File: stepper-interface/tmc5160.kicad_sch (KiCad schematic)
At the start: 30 parts, among them J401 Molex_Pico-SPOX_Horizontal, J402 Molex_Pico-Clasp_Horizontal, U401 TMC5160A-WA, U402 MAX6816, X401 16MHz

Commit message: First attempt at production files
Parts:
- C401, C403, C404, C408, C413, C417: Comment (none) -> 0.1 µF ±10% 100V Ceramic Capacitor X5R 0402 (1005 Metric)
- C402: Comment (none) -> 0.022 µF ±10% 100V Ceramic Capacitor X7R 0603 (1608 Metric)
- C405: Comment (none) -> 0.47 µF ±10% 35V Ceramic Capacitor X5R 0402 (1005 Metric)
- C406, C407: Comment (none) -> 2.2 µF ±10% 35V Ceramic Capacitor X5R 0402 (1005 Metric)
- C409, C410, C411, C412: Comment (none) -> 0.22 µF ±10% 25V Ceramic Capacitor X6S 0402 (1005 Metric)
- C414, C415: Comment (none) -> 2.2 µF ±10% 100V Ceramic Capacitor X7T 0805 (2012 Metric)
- C416: Comment (none) -> 220 µF 50 V Aluminum - Polymer Capacitors Radial, Can - SMD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
- D401: Comment (none) -> 77.4V Clamp 2.6A Ipp Tvs Diode Surface Mount SOD-123F; Package (none) -> SOD-123F
- J401: Comment (none) -> Connector Header Surface Mount, Right Angle 4 position 0.05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
- J402: Comment (none) -> Connector Header Surface Mount, Right Angle 2 position 0.03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
- R401: Comment (none) -> 2.2 Ohms ±5% 0.1W, 1/10W Chip Resistor 0402 (1005 Metric) A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
- R402, R403, R406, R407: Comment (none) -> 47 Ohms ±1% 0.063W, 1/16W Chip Resistor 0402 (1005 Metric) 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
- R404, R405: Comment (none) -> 150 mOhms ±1% 1W Chip Resistor 1206 (3216 Metric) Automotiv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
- U401: Comment (none) -> Bipolar Motor Driver Power MOSFET SPI, Step/Direction 56-QF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
- U402: Comment (none) -> Switch Debouncer SOT-143-4
- X401: Comment (none) -> 16 MHz XO (Standard) HCMOS Oscillator 3.3V Enable/Disable 4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
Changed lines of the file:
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@@
       (effects (font (size 1.524 1.524)) hide)
+    )
+    (property "Comment" "0.22 µF ±10% 25V Ceramic Capacitor X6S 0402 (1005 Metric)" (at 226.06 40.64 0)
+      (effects (font (size 1.27 1.27)) hide)
     )
     (pin "1")
@@
       (effects (font (size 1.524 1.524)) hide)
     )
+    (property "Comment" "47 Ohms ±1% 0.063W, 1/16W Chip Resistor 0402 (1005 Metric) Automotive AEC-Q200 Thick Film" (at 97.79 129.54 0)
+      (effects (font (size 1.27 1.27)) hide)
+    )
     (pin "1")
     (pin "2")
@@
       (effects (font (size 1.524 1.524)) hide)
     )
+    (property "Comment" "0.1 µF ±10% 100V Ceramic Capacitor X5R 0402 (1005 Metric)" (at 187.96 40.64 0)
+      (effects (font (size 1.27 1.27)) hide)
+    )
     (pin "2")
     (pin "1")
@@
     (property "Synopsis" "CAP CER 0.22UF 25V X6S" (at 208.28 30.48 0)
       (effects (font (size 1.524 1.524)) hide)
+    )
+    (property "Comment" "0.22 µF ±10% 25V Ceramic Capacitor X6S 0402 (1005 Metric)" (at 200.66 40.64 0)
+      (effects (font (size 1.27 1.27)) hide)
     )
     (pin "1")
@@
       (effects (font (size 1.524 1.524)) hide)
     )
+    (property "Comment" "2.2 µF ±10% 35V Ceramic Capacitor X5R 0402 (1005 Metric)" (at 162.56 40.64 0)
+      (effects (font (size 1.27 1.27)) hide)
+    )
     (pin "2")
     (pin "1")
@@
       (effects (font (size 1.27 1.27)) hide)
     )
+    (property "Comment" "Connector Header Surface Mount, Right Angle 4 position 0.059\" (1.50mm)" (at 276.86 125.73 0)
+      (effects (font (size 1.27 1.27)) hide)
+    )
     (pin "1")
     (pin "2")
@@
     (property "Synopsis" "IC SWITCH DEBOUNCER" (at 54.61 191.77 0)
       (effects (font (size 1.524 1.524)) hide)
+    )
+    (property "Comment" "Switch Debouncer SOT-143-4" (at 54.61 175.26 0)
+      (effects (font (size 1.27 1.27)) hide)
     )
     (pin "1")
@@
       (effects (font (size 1.524 1.524)) hide)
     )
+    (property "Comment" "0.1 µF ±10% 100V Ceramic Capacitor X5R 0402 (1005 Metric)" (at 48.26 40.64 0)
+      (effects (font (size 1.27 1.27)) hide)
+    )
     (pin "2")
     (pin "1")
@@
       (effects (font (size 1.524 1.524)) hide)
     )
+    (property "Comment" "0.22 µF ±10% 25V Ceramic Capacitor X6S 0402 (1005 Metric)" (at 213.36 40.64 0)
+      (effects (font (size 1.27 1.27)) hide)
+    )
     (pin "1")
     (pin "2")
@@
     (property "Synopsis" "CAP CER 0.1UF 100V X5R" (at 170.18 55.88 0)
       (effects (font (size 1.524 1.524)) hide)
+    )
+    (property "Comment" "0.1 µF ±10% 100V Ceramic Capacitor X5R 0402 (1005 Metric)" (at 162.56 66.04 0)
+      (effects (font (size 1.27 1.27)) hide)
     )
     (pin "2")
@@
     )
     (property "Synopsis" "IC MTR DRVR BIPOLAR 8-60V" (at 54.61 109.22 0)
+      (effects (font (size 1.27 1.27)) hide)
+    )
+    (property "Comment" "Bipolar Motor Driver Power MOSFET SPI, Step/Direction 56-QFN (8x8)" (at 54.61 109.22 0)
       (effects (font (size 1.27 1.27)) hide)
     )
@@
       (effects (font (size 1.524 1.524)) hide)
     )
+    (property "Comment" "0.022 µF ±10% 100V Ceramic Capacitor X7R 0603 (1608 Metric)" (at 99.06 40.64 0)
+      (effects (font (size 1.27 1.27)) hide)
+    )
     (pin "1")
     (pin "2")
@@
       (effects (font (size 1.524 1.524)) hide)
     )
+    (property "Comment" "2.2 µF ±10% 100V Ceramic Capacitor X7T 0805 (2012 Metric)" (at 187.96 66.04 0)
+      (effects (font (size 1.27 1.27)) hide)
+    )
     (pin "2")
     (pin "1")
@@
       (effects (font (size 1.524 1.524)) hide)
     )
+    (property "Comment" "47 Ohms ±1% 0.063W, 1/16W Chip Resistor 0402 (1005 Metric) Automotive AEC-Q200 Thick Film" (at 97.79 111.76 0)
+      (effects (font (size 1.27 1.27)) hide)
+    )
     (pin "1")
     (pin "2")
@@
       (effects (font (size 1.524 1.524)) hide)
     )
+    (property "Comment" "150 mOhms ±1% 1W Chip Resistor 1206 (3216 Metric) Automotive AEC-Q200, Current Sense Thick Film" (at 106.68 120.65 0)
+      (effects (font (size 1.27 1.27)) hide)
+    )
     (pin "2")
     (pin "1")
@@
     )
     (property "Vendor Part Number" "F5832CT-ND" (at 149.86 66.04 0)
+      (effects (font (size 1.27 1.27)) hide)
+    )
+    (property "Comment" "77.4V Clamp 2.6A Ipp Tvs Diode Surface Mount SOD-123F" (at 149.86 66.04 0)
+      (effects (font (size 1.27 1.27)) hide)
+    )
+    (property "Package" " SOD-123F" (at 149.86 66.04 0)
       (effects (font (size 1.27 1.27)) hide)
     )
@@
     )
     (property "Synopsis" "XTAL OSC XO 16.0000MHZ HCMOS SMD" (at 71.12 40.64 0)
+      (effects (font (size 1.27 1.27)) hide)
+    )
+    (property "Comment" "16 MHz XO (Standard) HCMOS Oscillator 3.3V Enable/Disable 4-SMD, No Lead" (at 71.12 40.64 0)
       (effects (font (size 1.27 1.27)) hide)
     )
@@
       (effects (font (size 1.27 1.27)) hide)
     )
+    (property "Comment" "Connector Header Surface Mount, Right Angle 2 position 0.039\" (1.00mm)" (at 101.6 177.8 0)
+      (effects (font (size 1.27 1.27)) hide)
+    )
     (pin "2")
     (pin "1")
@@
       (effects (font (size 1.524 1.524)) hide)
     )
+    (property "Comment" "47 Ohms ±1% 0.063W, 1/16W Chip Resistor 0402 (1005 Metric) Automotive AEC-Q200 Thick Film" (at 128.27 111.76 0)
+      (effects (font (size 1.27 1.27)) hide)
+    )
     (pin "1")
     (pin "2")
@@
       (effects (font (size 1.524 1.524)) hide)
     )
+    (property "Comment" "0.47 µF ±10% 35V Ceramic Capacitor X5R 0402 (1005 Metric)" (at 137.16 40.64 0)
+      (effects (font (size 1.27 1.27)) hide)
+    )
     (pin "2")
     (pin "1")
@@
       (effects (font (size 1.27 1.27)) hide)
     )
+    (property "Comment" "220 µF 50 V Aluminum - Polymer Capacitors Radial, Can - SMD 13mOhm 4000 Hrs @ 125°C" (at 200.66 66.04 0)
+      (effects (font (size 1.27 1.27)) hide)
+    )
     (pin "1")
     (pin "2")
@@
     (property "Synopsis" "CAP CER 0.22UF 25V X6S" (at 246.38 30.48 0)
       (effects (font (size 1.524 1.524)) hide)
+    )
+    (property "Comment" "0.22 µF ±10% 25V Ceramic Capacitor X6S 0402 (1005 Metric)" (at 238.76 40.64 0)
+      (effects (font (size 1.27 1.27)) hide)
     )
     (pin "1")
@@
       (effects (font (size 1.524 1.524)) hide)
     )
+    (property "Comment" "47 Ohms ±1% 0.063W, 1/16W Chip Resistor 0402 (1005 Metric) Automotive AEC-Q200 Thick Film" (at 128.27 129.54 0)
+      (effects (font (size 1.27 1.27)) hide)
+    )
     (pin "1")
     (pin "2")
@@
       (effects (font (size 1.524 1.524)) hide)
     )
+    (property "Comment" "2.2 Ohms ±5% 0.1W, 1/10W Chip Resistor 0402 (1005 Metric) Automotive AEC-Q200 Thick Film" (at 149.86 40.64 0)
+      (effects (font (size 1.27 1.27)) hide)
+    )
     (pin "1")
     (pin "2")
@@
     (property "Synopsis" "CAP CER 0.1UF 100V X5R" (at 132.08 30.48 0)
       (effects (font (size 1.524 1.524)) hide)
+    )
+    (property "Comment" "0.1 µF ±10% 100V Ceramic Capacitor X5R 0402 (1005 Metric)" (at 124.46 40.64 0)
+      (effects (font (size 1.27 1.27)) hide)
     )
     (pin "2")
@@
       (effects (font (size 1.524 1.524)) hide)
     )
+    (property "Comment" "150 mOhms ±1% 1W Chip Resistor 1206 (3216 Metric) Automotive AEC-Q200, Current Sense Thick Film" (at 137.16 120.65 0)
+      (effects (font (size 1.27 1.27)) hide)
+    )
     (pin "2")
     (pin "1")
@@
       (effects (font (size 1.524 1.524)) hide)
     )
+    (property "Comment" "2.2 µF ±10% 35V Ceramic Capacitor X5R 0402 (1005 Metric)" (at 175.26 40.64 0)
+      (effects (font (size 1.27 1.27)) hide)
+    )
     (pin "2")
     (pin "1")
@@
       (effects (font (size 1.524 1.524)) hide)
     )
+    (property "Comment" "2.2 µF ±10% 100V Ceramic Capacitor X7T 0805 (2012 Metric)" (at 175.26 66.04 0)
+      (effects (font (size 1.27 1.27)) hide)
+    )
     (pin "2")
     (pin "1")
@@
     (property "Synopsis" "CAP CER 0.1UF 100V X5R" (at 119.38 30.48 0)
       (effects (font (size 1.524 1.524)) hide)
+    )
+    (property "Comment" "0.1 µF ±10% 100V Ceramic Capacitor X5R 0402 (1005 Metric)" (at 111.76 40.64 0)
+      (effects (font (size 1.27 1.27)) hide)
     )
     (pin "2")
@@
       (effects (font (size 1.524 1.524)) hide)
     )
-    (pin "2")
+    (property "Comment" "0.1 µF ±10% 100V Ceramic Capacitor X5R 0402 (1005 Metric)" (at 25.4 175.26 0)
+      (effects (font (size 1.27 1.27)) hide)
+    )
+    (pin "2")

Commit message: Update schematic fields
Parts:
- C401, C403, C404, C408, C413, C417: Comment 0.1 µF ±10% 100V Ceramic Capacitor X5R 0402 (1005 Metric) -> Murata Electronics GRM155R62A104KE14D 0.1 µF ±10% 100V Cera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; LCSC (none) -> C162178
- C402: Comment 0.022 µF ±10% 100V Ceramic Capacitor X7R 0603 (1608 Metric) -> Murata Electronics GCM188R72A223KA37D 0.022 µF ±10% 100V Ce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; LCSC (none) -> C161234
- C405: Comment 0.47 µF ±10% 35V Ceramic Capacitor X5R 0402 (1005 Metric) -> Murata Electronics GRT155R6YA474KE01D 0.47 µF ±10% 35V Cera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; LCSC (none) -> C711580
- C406, C407: Comment 2.2 µF ±10% 35V Ceramic Capacitor X5R 0402 (1005 Metric) -> TDK Corporation C1005X5R1V225K050BC 2.2 µF ±10% 35V Ceramic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; LCSC (none) -> C2167643
- C409, C410, C411, C412: Comment 0.22 µF ±10% 25V Ceramic Capacitor X6S 0402 (1005 Metric) -> Murata Electronics GRT155C81E224KE01D 0.22 µF ±10% 25V Cera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; LCSC (none) -> C126623
- C414, C415: Comment 2.2 µF ±10% 100V Ceramic Capacitor X7T 0805 (2012 Metric) -> Murata Electronics GRT21BD72A225KE13K 2.2 µF ±10% 100V Cera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
- C416: Comment 220 µF 50 V Aluminum - Polymer Capacitors Radial, Can - SMD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 -> Panasonic Electronic Components EEH-ZS1H221V 220 µF 50 V Al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
- D401: Comment 77.4V Clamp 2.6A Ipp Tvs Diode Surface Mount SOD-123F -> Littelfuse Inc. SMF48A 77.4V Clamp 2.6A Ipp Tvs Diode Surfa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; LCSC (none) -> C1509577
- J401: Comment Connector Header Surface Mount, Right Angle 4 position 0.05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 -> Molex 0874380443 Connector Header Surface Mount, Right Angl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; LCSC (none) -> C564208
- J402: Comment Connector Header Surface Mount, Right Angle 2 position 0.03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 -> Molex 5015680207 Connector Header Surface Mount, Right Angl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; LCSC (none) -> C505123
- R401: Comment 2.2 Ohms ±5% 0.1W, 1/10W Chip Resistor 0402 (1005 Metric) A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 -> Panasonic Electronic Components ERJ-2GEJ2R2X 2.2 Ohms ±5% 0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
- R402, R403, R406, R407: Comment 47 Ohms ±1% 0.063W, 1/16W Chip Resistor 0402 (1005 Metric) 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 -> Stackpole Electronics Inc RMCF0402FT47R0 47 Ohms ±1% 0.063W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; LCSC (none) -> C2479306
- R404, R405: Comment 150 mOhms ±1% 1W Chip Resistor 1206 (3216 Metric) Automotiv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 -> Delta Electronics/Cyntec VSRP1206S1-R150F 150 mOhms ±1% 1W 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; LCSC (none) -> C4090676
- U401: Comment Bipolar Motor Driver Power MOSFET SPI, Step/Direction 56-QF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 -> Analog Devices Inc. TMC5160A-WA Bipolar Motor Driver Power 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; LCSC (none) -> C1161714
- U402: Comment Switch Debouncer SOT-143-4 -> Analog Devices Inc./Maxim Integrated MAX6816EUS+T Switch De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; LCSC (none) -> C41637
- X401: Comment 16 MHz XO (Standard) HCMOS Oscillator 3.3V Enable/Disable 4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 -> ECS Inc. ECS-2520S33-160-FN-TR 16 MHz XO (Standard) HCMOS O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; LCSC (none) -> C2451298

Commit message: Add jlcpcb fabrication files
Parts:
- J402: Manufactuer Part Number 5015680207 -> (none); Manufacturer Part Number (none) -> 5015680207
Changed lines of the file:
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@@
       (effects (font (size 1.27 1.27)) hide)
     )
-    (property "Manufactuer Part Number" "5015680207" (at 101.6 203.2 0)
+    (property "Manufacturer Part Number" "5015680207" (at 101.6 203.2 0)
       (effects (font (size 1.27 1.27)) hide)
     )

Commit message: Update LCSC part numbers
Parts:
- C414, C415: Comment Murata Electronics GRT21BD72A225KE13K 2.2 µF ±10% 100V Cera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 -> Murata Electronics GRM21BD72A225KE01L 2.2 µF ±10% 100V Cera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; LCSC (none) -> C2981733; Manufacturer Part Number GRT21BD72A225KE13K -> GRM21BD72A225KE01L; Vendor Part Number 490-GRT21BD72A225KE13KCT-ND -> 490-GRM21BD72A225KE01LCT-ND
- C416: LCSC (none) -> C454279
- R401: LCSC (none) -> C412897
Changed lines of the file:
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@@
   (title_block
     (title "stepper-interface")
-    (date "2024-05-08")
+    (date "2024-05-09")
     (rev "1.0")
     (company "Howard Hughes Medical Institute")
@@
       (effects (font (size 1.524 1.524)) hide)
     )
-    (property "Vendor Part Number" "490-GRT21BD72A225KE13KCT-ND" (at 193.04 58.42 0)
+    (property "Vendor Part Number" "490-GRM21BD72A225KE01LCT-ND" (at 193.04 58.42 0)
       (effects (font (size 1.524 1.524)) hide)
     )
@@
       (effects (font (size 1.27 1.27)) hide)
     )
-    (property "Manufacturer Part Number" "GRT21BD72A225KE13K" (at 187.96 66.04 0)
+    (property "Manufacturer Part Number" "GRM21BD72A225KE01L" (at 187.96 66.04 0)
       (effects (font (size 1.27 1.27)) hide)
     )
@@
       (effects (font (size 1.524 1.524)) hide)
     )
-    (property "Comment" "Murata Electronics GRT21BD72A225KE13K 2.2 µF ±10% 100V Ceramic Capacitor X7T 0805 (2012 Metric)" (at 187.96 66.04 0)
-      (effects (font (size 1.27 1.27)) hide)
-    )
-    (property "LCSC" "" (at 187.96 66.04 0)
+    (property "Comment" "Murata Electronics GRM21BD72A225KE01L 2.2 µF ±10% 100V Ceramic Capacitor X7T 0805 (2012 Metric)" (at 187.96 66.04 0)
+      (effects (font (size 1.27 1.27)) hide)
+    )
+    (property "LCSC" "C2981733" (at 187.96 66.04 0)
       (effects (font (size 1.27 1.27)) hide)
     )
@@
       (effects (font (size 1.27 1.27)) hide)
     )
-    (property "LCSC" "" (at 200.66 66.04 0)
+    (property "LCSC" "C454279" (at 200.66 66.04 0)
       (effects (font (size 1.27 1.27)) hide)
     )
@@
       (effects (font (size 1.27 1.27)) hide)
     )
-    (property "LCSC" "" (at 149.86 40.64 0)
+    (property "LCSC" "C412897" (at 149.86 40.64 0)
       (effects (font (size 1.27 1.27)) hide)
     )
@@
       (effects (font (size 1.524 1.524)) hide)
     )
-    (property "Vendor Part Number" "490-GRT21BD72A225KE13KCT-ND" (at 180.34 58.42 0)
+    (property "Vendor Part Number" "490-GRM21BD72A225KE01LCT-ND" (at 180.34 58.42 0)
       (effects (font (size 1.524 1.524)) hide)
     )
@@
       (effects (font (size 1.27 1.27)) hide)
     )
-    (property "Manufacturer Part Number" "GRT21BD72A225KE13K" (at 175.26 66.04 0)
+    (property "Manufacturer Part Number" "GRM21BD72A225KE01L" (at 175.26 66.04 0)
       (effects (font (size 1.27 1.27)) hide)
     )
@@
       (effects (font (size 1.524 1.524)) hide)
     )
-    (property "Comment" "Murata Electronics GRT21BD72A225KE13K 2.2 µF ±10% 100V Ceramic Capacitor X7T 0805 (2012 Metric)" (at 175.26 66.04 0)
-      (effects (font (size 1.27 1.27)) hide)
-    )
-    (property "LCSC" "" (at 175.26 66.04 0)
-      (effects (font (size 1.27 1.27)) hide)
-    )
+    (property "Comment" "Murata Electronics GRM21BD72A225KE01L 2.2 µF ±10% 100V Ceramic Capacitor X7T 0805 (2012 Metric)" (at 175.26 66.04 0)
+      (effects (font (size 1.27 1.27)) hide)
+    )
+    (property "LCSC" "C2981733" (at 175.26 66.04 0)
+      (effects (font (size 1.27 1.27)) hide)
+    )

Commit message: Switch LEDs
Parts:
- C401, C403, C404, C408, C413, C417: Comment Murata Electronics GRM155R62A104KE14D 0.1 µF ±10% 100V Cera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 -> (none)
- C402: Comment Murata Electronics GCM188R72A223KA37D 0.022 µF ±10% 100V Ce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 -> (none)
- C405: Comment Murata Electronics GRT155R6YA474KE01D 0.47 µF ±10% 35V Cera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 -> (none)
- C406, C407: Comment TDK Corporation C1005X5R1V225K050BC 2.2 µF ±10% 35V Ceramic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 -> (none)
- C409, C410, C411, C412: Comment Murata Electronics GRT155C81E224KE01D 0.22 µF ±10% 25V Cera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 -> (none)
- C414, C415: Comment Murata Electronics GRM21BD72A225KE01L 2.2 µF ±10% 100V Cera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 -> (none)
- C416: Comment Panasonic Electronic Components EEH-ZS1H221V 220 µF 50 V Al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 -> (none)
- D401: Comment Littelfuse Inc. SMF48A 77.4V Clamp 2.6A Ipp Tvs Diode Surfa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 -> (none)
- J401: Comment Molex 0874380443 Connector Header Surface Mount, Right Angl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 -> (none)
- J402: Comment Molex 5015680207 Connector Header Surface Mount, Right Angl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 -> (none)
- R401: Comment Panasonic Electronic Components ERJ-2GEJ2R2X 2.2 Ohms ±5% 0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 -> (none)
- R402, R403, R406, R407: Comment Stackpole Electronics Inc RMCF0402FT47R0 47 Ohms ±1% 0.063W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 -> (none)
- R404, R405: Comment Delta Electronics/Cyntec VSRP1206S1-R150F 150 mOhms ±1% 1W 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 -> (none)
- U401: Comment Analog Devices Inc. TMC5160A-WA Bipolar Motor Driver Power 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 -> (none)
- U402: Comment Analog Devices Inc./Maxim Integrated MAX6816EUS+T Switch De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 -> (none)
- X401: Comment ECS Inc. ECS-2520S33-160-FN-TR 16 MHz XO (Standard) HCMOS O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 -> (none)

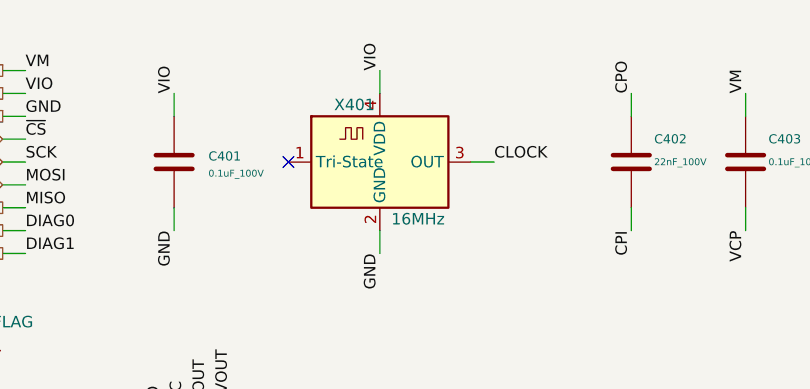
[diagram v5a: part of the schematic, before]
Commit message: Update parts based on jlcpcb availability
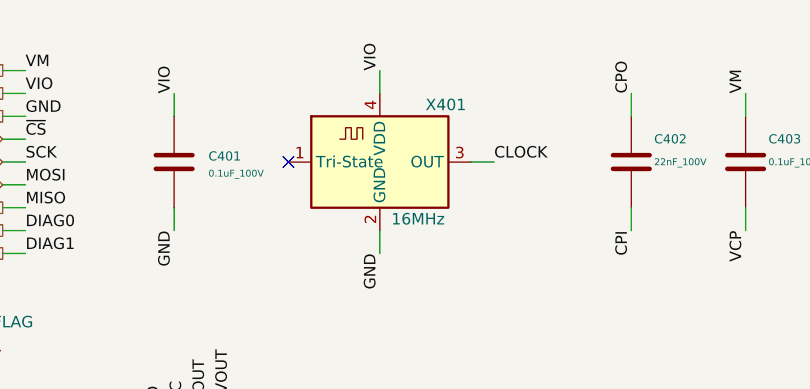
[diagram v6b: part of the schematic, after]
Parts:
- C416: Package (none) -> SMD_D10xL16.8mm
- D401: Package SOD-123F -> SOD-123FL
- J401: Package (none) -> SMD
- J402: Package (none) -> SMD_P=1mm
- U401: Package 47-VFQFN Exposed Pad -> QFN-56-EP(8x8)
- U402: Package SOT143-4 -> SOT-143
- X401: Package (none) -> SMD2520-4P
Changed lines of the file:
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@@
+      (effects (font (size 1.27 1.27)) hide)
+    )
+    (property "Package" "SMD" (at 276.86 125.73 0)
       (effects (font (size 1.27 1.27)) hide)
     )
@@
       (effects (font (size 1.524 1.524)))
     )
-    (property "Package" " SOT143-4" (at 54.61 175.26 0)
+    (property "Package" "SOT-143" (at 54.61 175.26 0)
       (effects (font (size 1.524 1.524)) hide)
     )
@@
       (effects (font (size 1.27 1.27)) hide)
     )
-    (property "Package" "47-VFQFN Exposed Pad" (at 54.61 109.22 0)
+    (property "Package" "QFN-56-EP(8x8)" (at 54.61 109.22 0)
       (effects (font (size 1.27 1.27)) hide)
     )
@@
       (effects (font (size 1.27 1.27)) hide)
     )
-    (property "Package" " SOD-123F" (at 149.86 66.04 0)
+    (property "Package" "SOD-123FL" (at 149.86 66.04 0)
       (effects (font (size 1.27 1.27)) hide)
     )
@@
   (symbol (lib_id "Janelia:Oscillator_16MHz_ECS-2520S33") (at 71.12 40.64 0) (unit 1)
     (in_bom yes) (on_board yes) (dnp no)
-    (property "Reference" "X401" (at 66.04 34.29 0)
+    (property "Reference" "X401" (at 76.2 34.29 0)
       (effects (font (size 1.27 1.27)) (justify left))
     )
@@
     )
     (property "LCSC" "C2451298" (at 71.12 40.64 0)
+      (effects (font (size 1.27 1.27)) hide)
+    )
+    (property "Package" "SMD2520-4P" (at 71.12 40.64 0)
       (effects (font (size 1.27 1.27)) hide)
     )
@@
       (effects (font (size 1.27 1.27)) hide)
     )
+    (property "Package" "SMD_P=1mm" (at 101.6 177.8 0)
+      (effects (font (size 1.27 1.27)) hide)
+    )
     (pin "2")
     (pin "1")
@@
       (effects (font (size 1.27 1.27)) hide)
     )
+    (property "Package" "SMD_D10xL16.8mm" (at 200.66 66.04 0)
+      (effects (font (size 1.27 1.27)) hide)
+    )
